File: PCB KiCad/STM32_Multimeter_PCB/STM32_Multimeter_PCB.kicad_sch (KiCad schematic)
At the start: 52 parts, among them J1 Conn_01x02_Pin, J2 USB_B_Micro, J3 Conn_01x04_Pin, J4 Conn_Coaxial, J5 Conn_01x03_Pin, SW1 SW_Push, SW2 SW_DIP_x01, SW3 SW_Push, U1 STM32WB55CGUx, U3 LTC4054XES5-4.2, U4 DW01A, U5 FS8205A, Y1 Crystal 32 MHz

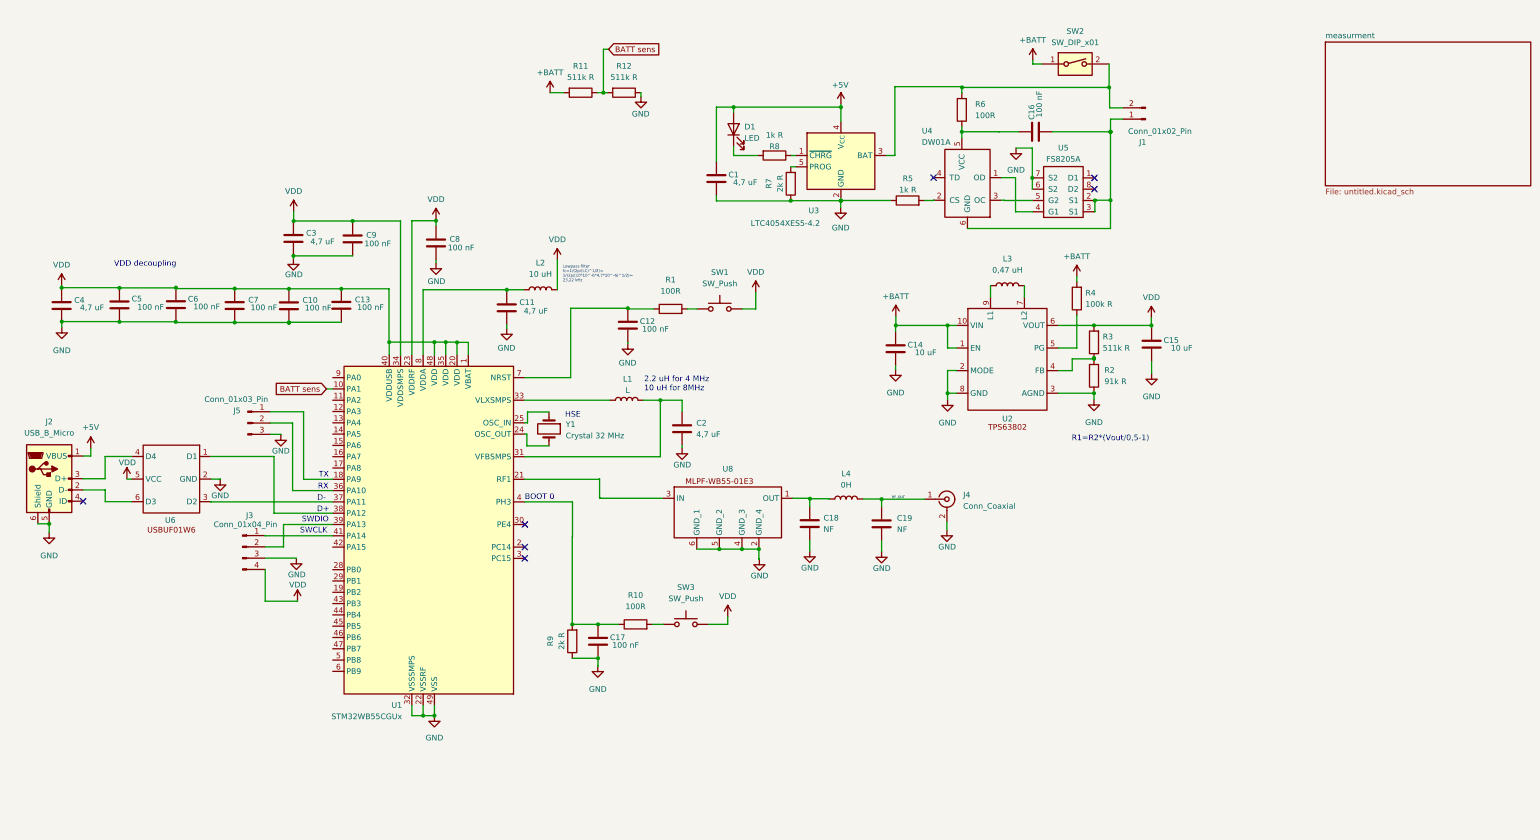
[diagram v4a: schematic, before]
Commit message: Added 9V SMPS, swiched 3,3V SMPS to linnear regulator
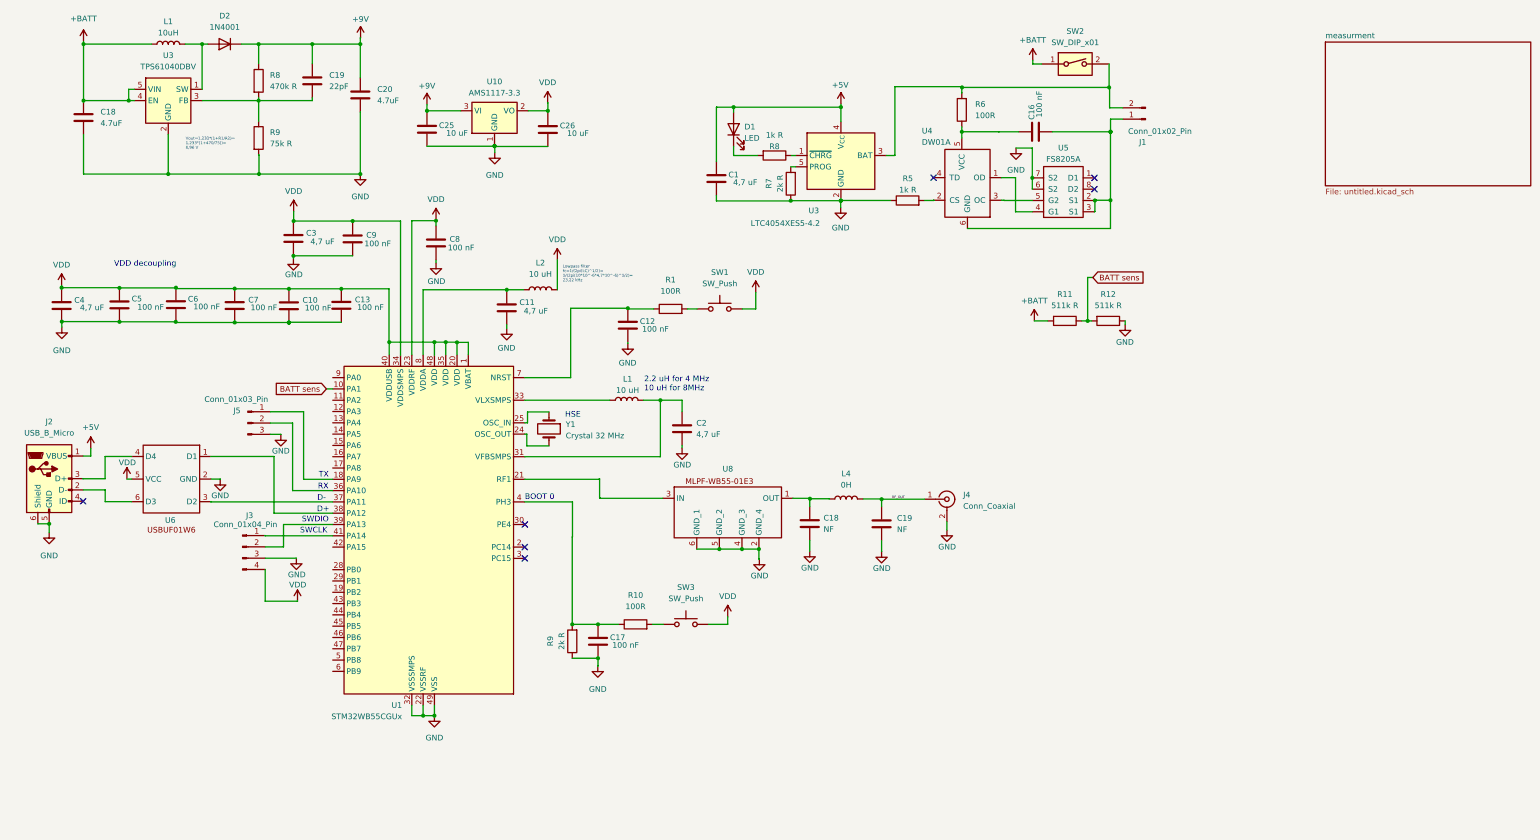
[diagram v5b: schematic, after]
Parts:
- removed C14, C15: 10 uF, symbol Device:C
- removed L3: 0,47 uH, symbol Device:L
- removed R2: 91k R, symbol Device:R
- removed R3: 511k R, symbol Device:R
- removed R4: 100k R, symbol Device:R
- removed U2: ~, symbol STM32_Bsed_Meter_Library:TSP63805
- added C18, C20: 4.7uF, Capacitor_SMD:C_0805_2012Metric_Pad1.18x1.45mm_HandSolder, symbol Device:C
- added C19: 22pF, Capacitor_SMD:C_0805_2012Metric_Pad1.18x1.45mm_HandSolder, symbol Device:C
- added C25, C26: 10 uF, Capacitor_SMD:C_0805_2012Metric, symbol Device:C
- added D2: 1N4001, Diode_SMD:D_SMA_Handsoldering, symbol Diode:1N4001
- added L1: 10uH, symbol Device:L
- added R8: 470k R, Resistor_SMD:R_0805_2012Metric_Pad1.20x1.40mm_HandSolder, symbol Device:R
- added R9: 75k R, Resistor_SMD:R_0805_2012Metric_Pad1.20x1.40mm_HandSolder, symbol Device:R
- added U10: AMS1117-3.3, Package_TO_SOT_SMD:SOT-223-3_TabPin2, symbol Regulator_Linear:AMS1117-3.3
- added U3: TPS61040DBV, Package_TO_SOT_SMD:SOT-23-5, symbol Regulator_Switching:TPS61040DBV
- C1, C10, C11, C12, C13, C16, C17, C18, C19, C2, C3, C4, C5, C6, C7, C8, C9: footprint (none) -> Capacitor_SMD:C_0805_2012Metric
- D1: footprint (none) -> LED_SMD:LED_0805_2012Metric
- J3: footprint (none) -> Connector_PinHeader_2.54mm:PinHeader_1x04_P2.54mm_Vertical
- J5: footprint (none) -> Connector_PinHeader_2.54mm:PinHeader_1x03_P2.54mm_Vertical
- L1: value L -> 10 uH
- R1, R10, R11, R12, R5, R6, R7, R8, R9: footprint (none) -> Resistor_SMD:R_0805_2012Metric
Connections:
- net +BATT: now also C18.1, L1.1, U3.4 (EN), U3.5 (VIN)
- net GND: now also C18.2, C20.2, C25.1, C26.1, R9.2, U10.1 (GND), U3.2 (GND)
- net VDD: now also C26.2, U10.2 (VO)
- new net: D2.2 (A), L1.2, U3.1 (SW)
- new net: C19.2, R8.2, R9.1, U3.3 (FB)
- new net +9V: C19.1, C20.1, C25.2, D2.1 (K), R8.1, U10.3 (VI)
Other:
- note added: "Vout=1,233*(1+R1/R2)= 1,233*(1+470/75))= 8,96 V"
- note removed: "R1=R2*(Vout/0,5-1)"
- moved on the sheet: R11, R12

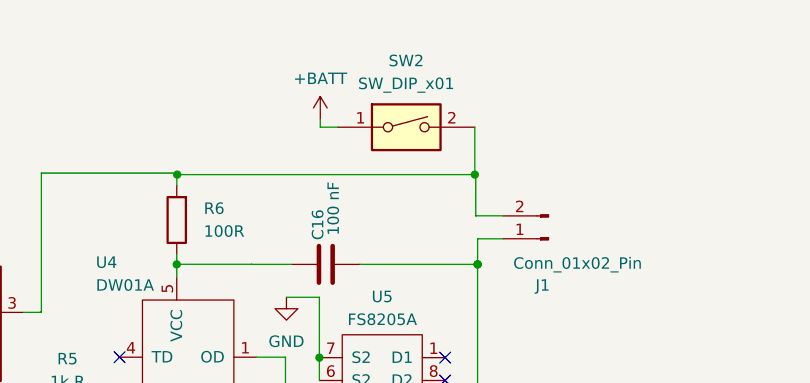
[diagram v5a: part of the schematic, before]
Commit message: Added component footprints
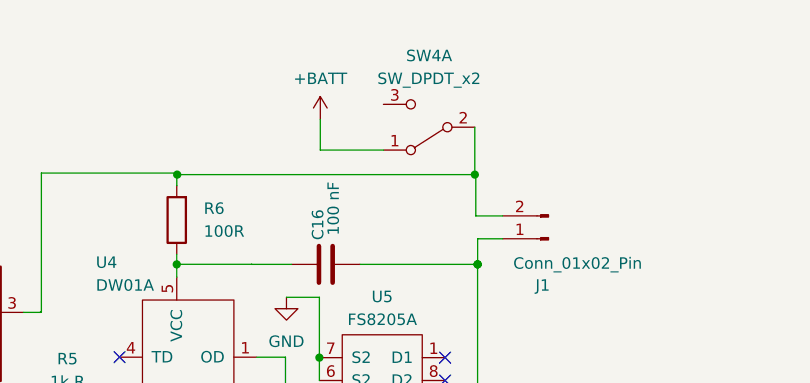
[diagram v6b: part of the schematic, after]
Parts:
- removed SW2: SW_DIP_x01, symbol Switch:SW_DIP_x01
- added SW4: SW_DPDT_x2, Connector_PinHeader_2.54mm:PinHeader_1x03_P2.54mm_Vertical, symbol Switch:SW_DPDT_x2
- J1: footprint (none) -> Connector_PinHeader_2.54mm:PinHeader_1x02_P2.54mm_Vertical
- J2: footprint (none) -> Connector_USB:USB_Micro-B_Wuerth_629105150521_CircularHoles
- L1, L2, L4: footprint (none) -> Inductor_SMD:L_Chilisin_BMRB00060650
- U6: footprint (none) -> Package_TO_SOT_SMD:SOT-363_SC-70-6_Handsoldering
- U8: footprint (none) -> moje_elementy:MLPF-WB55
- Y1: footprint (none) -> Crystal:Crystal_SMD_5032-2Pin_5.0x3.2mm_HandSoldering
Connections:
- net +BATT: now also SW4.1 (A)
- net at J1.2 (Pin_2), R6.2, U3.3 (BAT): now also SW4.2 (B)
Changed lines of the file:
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@@
-    (stroke (width 0) (type default))
-  )
-  (wire (pts (xy 243.5352 24.7396) (xy 245.4656 24.7396))
     (stroke (width 0) (type default))
   )
@@
     (stroke (width 0) (type default))
   )
+  (wire (pts (xy 243.5352 27.2796) (xy 243.5352 23.876))
+    (stroke (width 0) (type default))
+  )
   (wire (pts (xy 122.5804 44.6532) (xy 122.5804 43.1371))
     (stroke (width 0) (type default))
@@
     (stroke (width 0) (type default))
   )
-  (wire (pts (xy 243.5352 23.876) (xy 243.5352 24.7396))
+  (wire (pts (xy 250.5456 27.2796) (xy 243.5352 27.2796))
     (stroke (width 0) (type default))
   )
@@
       (effects (font (size 1.27 1.27)))
     )
-    (property "Footprint" "" (at 56.2356 125.6792 0)
+    (property "Footprint" "Package_TO_SOT_SMD:SOT-363_SC-70-6_Handsoldering" (at 56.2356 125.6792 0)
       (effects (font (size 1.27 1.27)) hide)
     )
@@
     )
   )
-  (symbol (lib_id "Switch:SW_DIP_x01") (at 253.0856 24.7396 0) (unit 1)
-    (in_bom yes) (on_board yes) (dnp no) (fields_autoplaced)
-    (property "Reference" "SW2" (at 253.0856 17.3736 0)
-      (effects (font (size 1.27 1.27)))
-    )
-    (property "Value" "SW_DIP_x01" (at 253.0856 19.9136 0)
-      (effects (font (size 1.27 1.27)))
-    )
-    (property "Footprint" "" (at 253.0856 24.7396 0)
-      (effects (font (size 1.27 1.27)) hide)
-    )
-    (property "Datasheet" "~" (at 253.0856 24.7396 0)
-      (effects (font (size 1.27 1.27)) hide)
-    )
-    (pin "1")
-    (pin "2")
-    (instances
-      (project "STM32_Multimeter_PCB"
-        (path "/841997f8-2aac-4d7b-a188-492c61267162"
-          (reference "SW2") (unit 1)
-        )
-      )
-    )
-  )
   (symbol (lib_id "Device:C") (at 30.1244 36.7792 0) (unit 1)
     (in_bom yes) (on_board yes) (dnp no) (fields_autoplaced)
@@
     )
   )
+  (symbol (lib_id "Switch:SW_DPDT_x2") (at 255.6256 24.7396 180) (unit 1)
+    (in_bom yes) (on_board yes) (dnp no) (fields_autoplaced)
+    (property "Reference" "SW4" (at 255.6256 16.8148 0)
+      (effects (font (size 1.27 1.27)))
+    )
+    (property "Value" "SW_DPDT_x2" (at 255.6256 19.3548 0)
+      (effects (font (size 1.27 1.27)))
+    )
+    (property "Footprint" "Connector_PinHeader_2.54mm:PinHeader_1x03_P2.54mm_Vertical" (at 255.6256 24.7396 0)
+      (effects (font (size 1.27 1.27)) hide)
+    )
+    (property "Datasheet" "~" (at 255.6256 24.7396 0)
+      (effects (font (size 1.27 1.27)) hide)
+    )
+    (pin "1")
+    (pin "2")
+    (pin "3")
+    (pin "4")
+    (pin "5")
+    (pin "6")
+    (instances
+      (project "STM32_Multimeter_PCB"
+        (path "/841997f8-2aac-4d7b-a188-492c61267162"
+          (reference "SW4") (unit 1)
+        )
+      )
+    )
+  )
   (symbol (lib_id "power:VDD") (at 25.1968 74.4728 0) (unit 1)
     (in_bom yes) (on_board yes) (dnp no) (fields_autoplaced)
@@
       (effects (font (size 1.27 1.27)))
     )
-    (property "Footprint" "" (at 268.8844 37.1348 0)
+    (property "Footprint" "Connector_PinHeader_2.54mm:PinHeader_1x02_P2.54mm_Vertical" (at 268.8844 37.1348 0)
       (effects (font (size 1.27 1.27)) hide)
     )
@@
       (effects (font (size 1.27 1.27)) (justify left))
     )
-    (property "Footprint" "" (at 134.7724 106.7816 0)
+    (property "Footprint" "Crystal:Crystal_SMD_5032-2Pin_5.0x3.2mm_HandSoldering" (at 134.7724 106.7816 0)
       (effects (font (size 1.27 1.27)) hide)
     )
@@
       (effects (font (size 1.27 1.27)))
     )
-    (property "Footprint" "" (at 132.842 75.4888 0)
+    (property "Footprint" "Inductor_SMD:L_Chilisin_BMRB00060650" (at 132.842 75.4888 0)
       (effects (font (size 1.27 1.27)) hide)
     )
@@
       (effects (font (size 1.27 1.27)))
     )
-    (property "Footprint" "" (at 26.2128 119.2276 0)
+    (property "Footprint" "Connector_USB:USB_Micro-B_Wuerth_629105150521_CircularHoles" (at 26.2128 119.2276 0)
       (effects (font (size 1.27 1.27)) hide)
     )
@@
       (effects (font (size 1.27 1.27)))
     )
-    (property "Footprint" "" (at 201.5744 122.5296 0)
+    (property "Footprint" "Inductor_SMD:L_Chilisin_BMRB00060650" (at 201.5744 122.5296 0)
       (effects (font (size 1.27 1.27)) hide)
     )
@@
       (effects (font (size 1.27 1.27)))
     )
-    (property "Footprint" "" (at 152.2476 100.33 0)
+    (property "Footprint" "Inductor_SMD:L_Chilisin_BMRB00060650" (at 152.2476 100.33 0)
       (effects (font (size 1.27 1.27)) hide)
     )
@@
       (effects (font (size 1.27 1.27)))
     )
-    (property "Footprint" "" (at 162.9156 131.2672 0)
+    (property "Footprint" "moje_elementy:MLPF-WB55" (at 162.9156 131.2672 0)
       (effects (font (size 1.27 1.27)) hide)
     )
@@
       (effects (font (size 1.27 1.27)))
     )
-    (property "Footprint" "" (at 49.1744 20.2692 0)
-      (effects (font (size 1.27 1.27)) hide)
-    )
+    (property "Footprint" "Inductor_SMD:L_Chilisin_BMRB00060650" (at 49.1744 20.2692 0)
+      (effects (font (size 1.27 1.27)) hide)
+    )

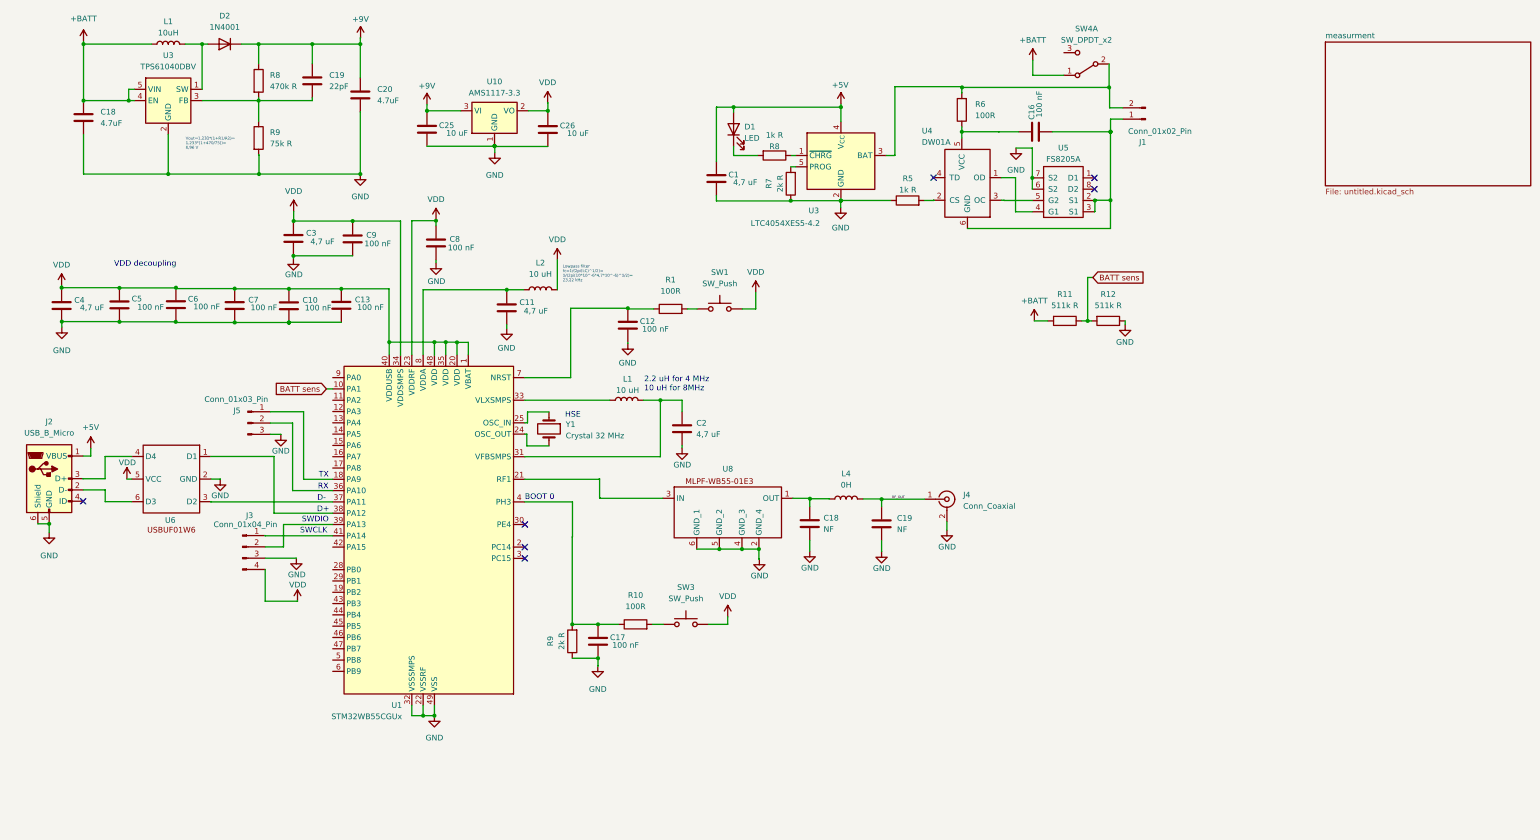
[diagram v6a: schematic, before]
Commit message: Connected measuring circuitry to STM32
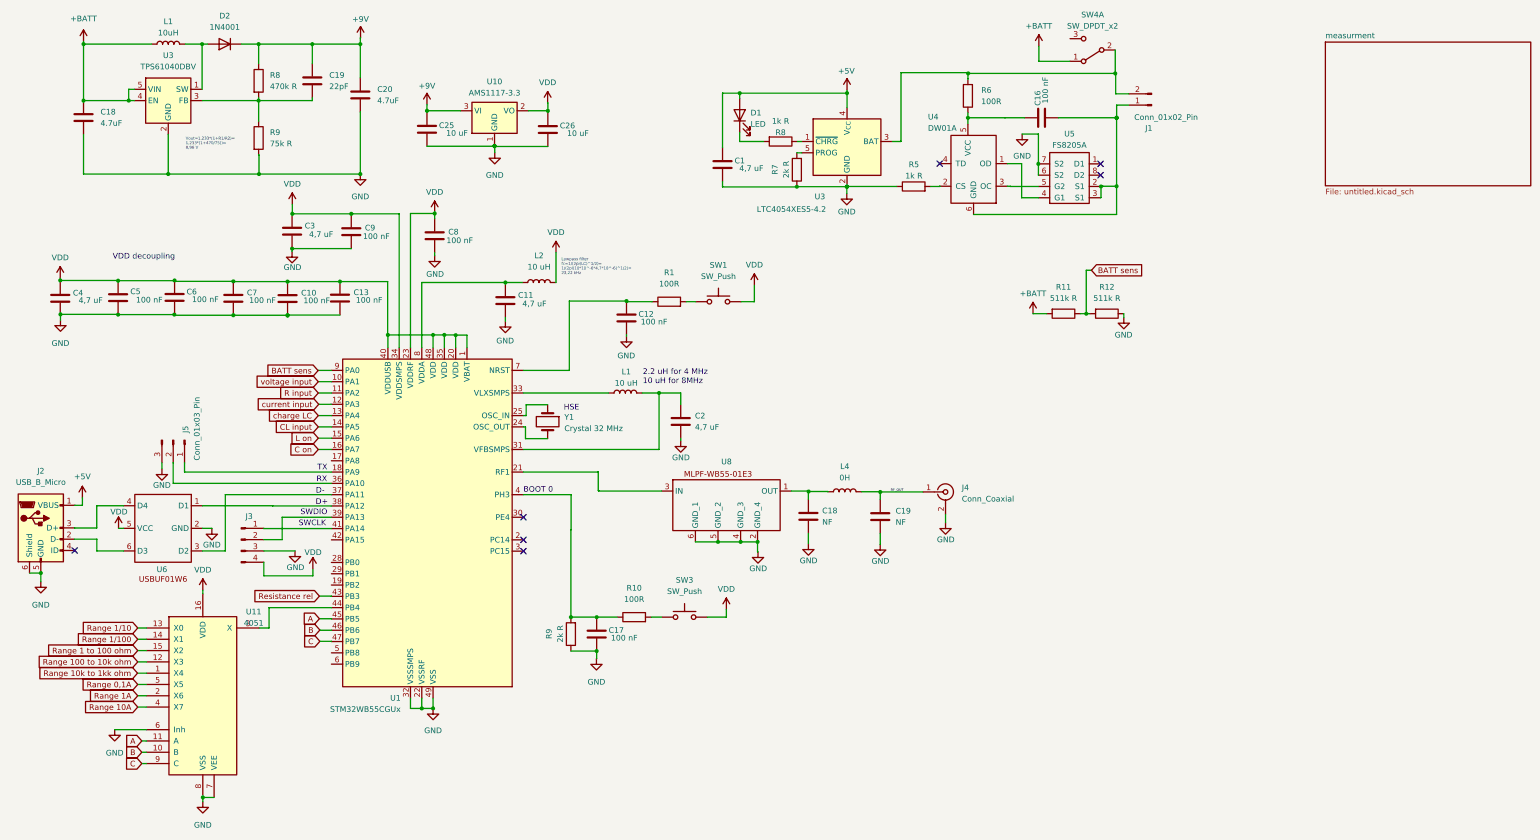
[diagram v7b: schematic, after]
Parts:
- added U11: 4051, Package_SO:SOP-16_4.4x10.4mm_P1.27mm, symbol 4xxx:4051
- L1, L2, L4: footprint Inductor_SMD:L_Chilisin_BMRB00060650 -> Inductor_SMD:L_Taiyo-Yuden_NR-50xx
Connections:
- net BATT sens: now also U1.9 (PA0); no longer U1.10 (PA1)
- net GND: now also U11.6 (Inh), U11.7 (VEE), U11.8 (VSS)
- net VDD: now also U11.16 (VDD)
- net R input: now reaches U1.11 (PA2)
- net current input: now reaches U1.12 (PA3)
- net charge LC: now reaches U1.13 (PA4)
- net CL input: now reaches U1.14 (PA5)
- net L on: now reaches U1.15 (PA6)
- net C on: now reaches U1.16 (PA7)
- net Resistance rel: now reaches U1.43 (PB3)
- net at U1.44 (PB4): now also U11.3 (X)
- net A: now reaches U1.45 (PB5)
- net A: now also U11.11 (A)
- net B: now reaches U1.46 (PB6)
- net B: now also U11.10 (B)
- net C: now reaches U1.47 (PB7)
- net C: now also U11.9 (C)
- new net Range 0,1A: U11.5 (X5)
- new net Range 1 to 100 ohm: U11.15 (X2)
- new net Range 100 to 10k ohm: U11.12 (X3)
- new net Range 10A: U11.4 (X7)
- new net Range 10k to 1kk ohm: U11.1 (X4)
- new net Range 1A: U11.2 (X6)
- new net Range 1/10: U11.13 (X0)
- new net Range 1/100: U11.14 (X1)
- new net voltage input: U1.10 (PA1)
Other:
- moved on the sheet: C1, C10, C11, C12, C13, C16, C17, C18, C19, C2, C3, C4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
